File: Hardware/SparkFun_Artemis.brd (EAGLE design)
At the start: 15 x 10 mm, 75 parts, among them J1 PAD.4X.6, J10 PAD.4X.6, J11 PAD.4X.6, J12 PAD.4X.6, J13 PAD.4X.6, J14 PAD.4X.6, J15 PAD.4X.6, J16 PAD.4X.6, J17 PAD.4X.6, J18 PAD.4X.6, J19 PAD.4X.6, J2 PAD.4X.6, J20 PAD.4X.6, J21 PAD.4X.6, J22 PAD.4X.6, J23 PAD.4X.6, J24 PAD.4X.6, J25 PAD.4X.6, J26 PAD.4X.6, J27 PAD.4X.6, J28 PAD.4X.6, J29 PAD.4X.6, J3 PAD.4X.6, J30 PAD.4X.6, J31 PAD.4X.6, J32 PAD.4X.6, J34 PAD.4X.6, J35 PAD.4X.6, J36 PAD.4X.6, J37 PAD.4X.6, J38 PAD.4X.6, J39 PAD.4X.6, J4 PAD.4X.6, J40 PAD.4X.6, J41 PAD.4X.6, J42 PAD.4X.6, J43 PAD.4X.6, J44 PAD.4X.6, J45 PAD.4X.6, J46 PAD.35X.35, J47 PAD.4X.6, J48 PAD.4X.6, J49 PAD.4X.6, J5 PAD.4X.6, J6 PAD.4X.6, J7 PAD.4X.6, J8 PAD.4X.6, J9 PAD.4X.6, U1 AMBIQ-APOLLO3KBR, Y1 32MHz

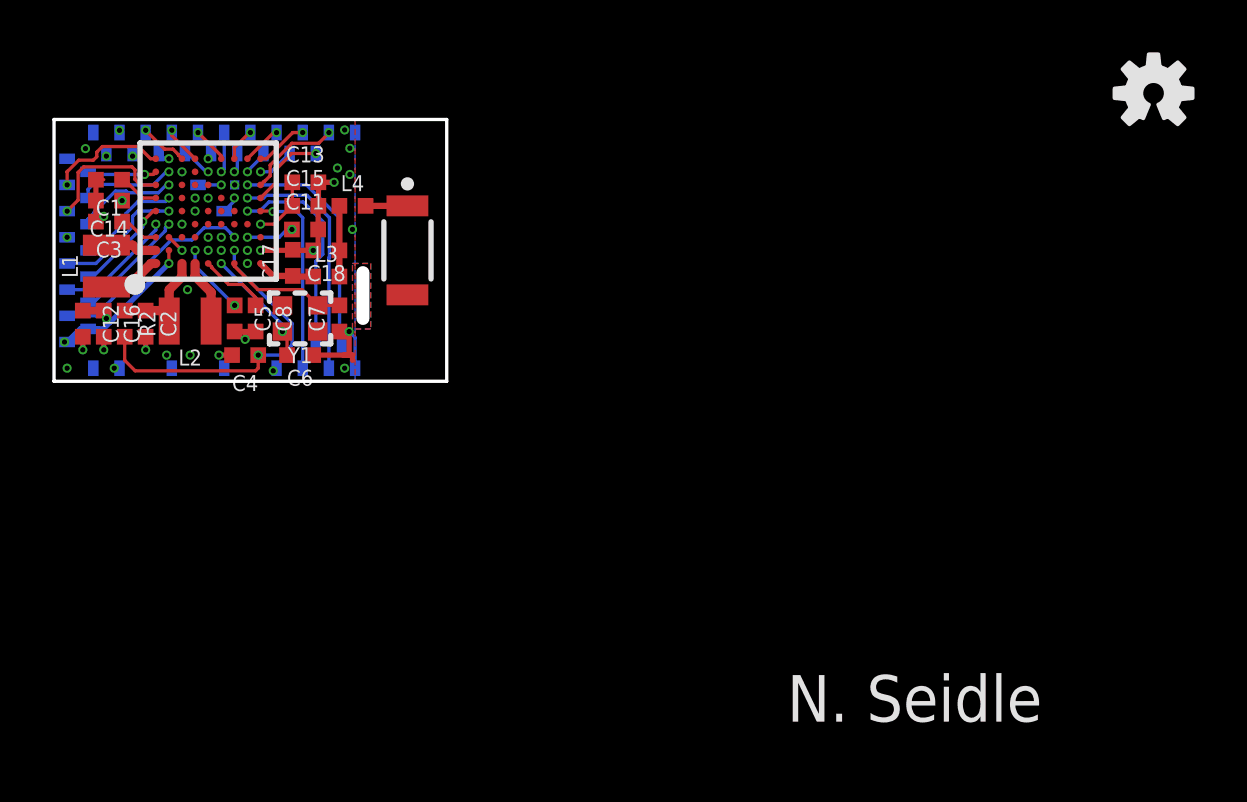
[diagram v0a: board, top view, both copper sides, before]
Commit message: Changing RF trace width to 11.55mil
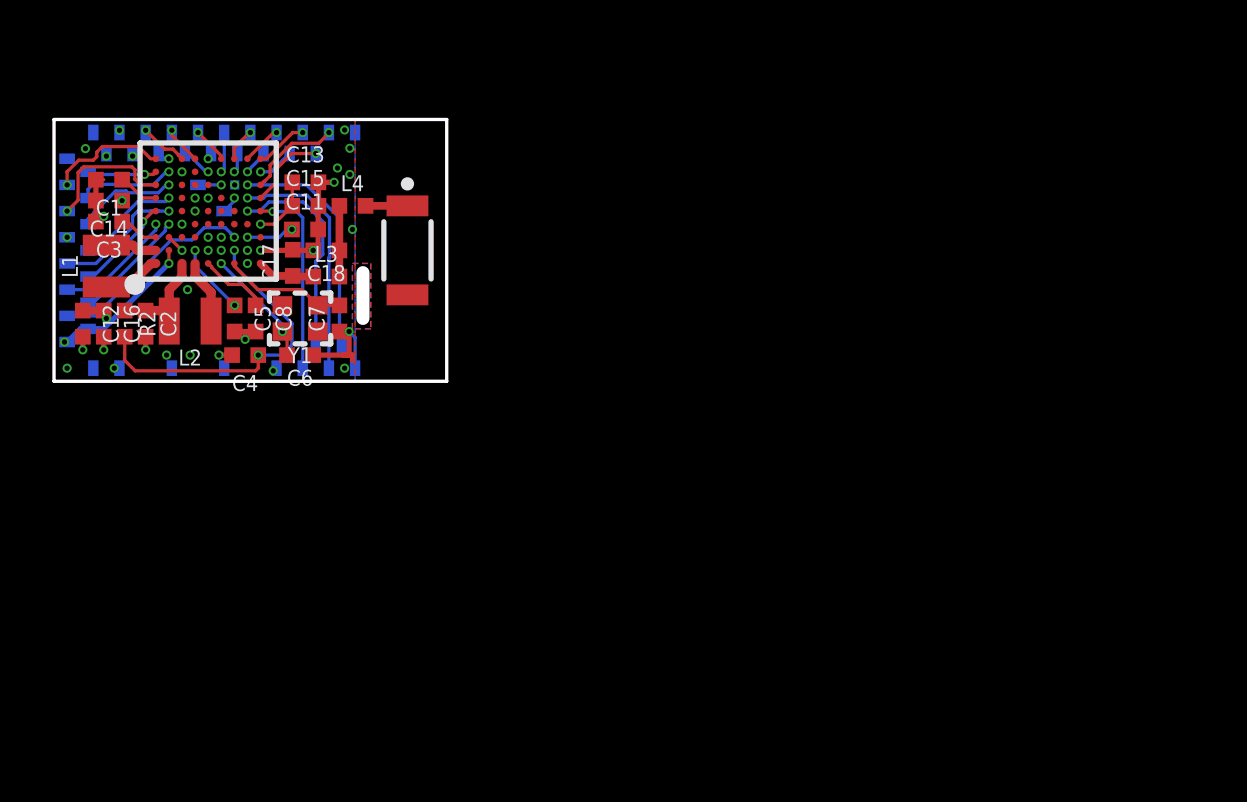
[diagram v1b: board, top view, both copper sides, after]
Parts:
- removed LOGO2: OSHW-LOGOS, SparkFun-Aesthetics:OSHW-LOGO-S
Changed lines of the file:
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@@
 <layer number="47" name="Measures" color="7" fill="1" visible="no" active="yes"/>
 <layer number="48" name="RF_Shield2" color="63" fill="1" visible="yes" active="yes"/>
-<layer number="49" name="Reference" color="7" fill="1" visible="yes" active="yes"/>
+<layer number="49" name="Reference" color="7" fill="1" visible="no" active="yes"/>
 <layer number="50" name="RF_Shield_Dimensions2" color="47" fill="1" visible="yes" active="yes"/>
 <layer number="51" name="tDocu" color="6" fill="1" visible="yes" active="yes"/>
@@
 <wire x1="11.8" y1="2.4" x2="11.8" y2="4.15" width="0.5" layer="46"/>
 <text x="40" y="5" size="1.778" layer="51" font="vector" ratio="15">0.8mm Thick FR4</text>
-<text x="28" y="-13" size="1.778" layer="21" font="vector" ratio="15">N. Seidle</text>
 <wire x1="0.4" y1="1" x2="0.4" y2="0.4" width="0.5" layer="48"/>
 <wire x1="0.4" y1="9.6" x2="0.4" y2="8.6" width="0.5" layer="48"/>
@@
 <wire x1="0.4" y1="0.4" x2="0.4" y2="9.6" width="0.05" layer="50"/>
 <text x="20.2" y="1.4" size="0.9" layer="50" font="vector" ratio="15">Alignment Leg Height: 1.8-1.9mm </text>
+<text x="27.559" y="-13.208" size="1.778" layer="51" font="vector" ratio="15">N. Seidle</text>
+<dimension x1="0.4" y1="1" x2="0.4" y2="0.4" x3="-2.3" y3="0.7" textsize="0.5" textratio="15" layer="50" width="0.05" unit="inch"/>
 </plain>
 <attributes>
@@
 <element name="J44" library="Module-Pads" package="MODULE_PAD" value="PAD.4X.6" x="0.5" y="8.5" smashed="yes" rot="MR0"/>
 <element name="LOGO1" library="SparkFun-Aesthetics" package="SFE_LOGO_FLAME_INTERNAL_0.05" value="SFE_LOGO_FLAME.05_INCH_INTERNAL" x="9.1" y="8.4" smashed="yes"/>
-<element name="LOGO2" library="SparkFun-Aesthetics" package="OSHW-LOGO-S" value="OSHW-LOGOS" x="42" y="11" smashed="yes"/>
 <element name="J46" library="Module-Pads" package="MODULE_MINI_PAD" value="PAD.35X.35" x="6.9" y="7.5" smashed="yes" rot="MR0"/>
 <element name="J45" library="Module-Pads" package="MODULE_PAD" value="PAD.4X.6" x="2.5" y="0.5" smashed="yes" rot="MR90"/>
@@
 <contactref element="C17" pad="1"/>
 <contactref element="L3" pad="1"/>
-<wire x1="7.888" y1="4.501" x2="8.366" y2="4.023" width="0.24" layer="1"/>
-<wire x1="8.366" y1="4.023" x2="9.121" y2="4.023" width="0.24" layer="1"/>
+<wire x1="7.888" y1="4.501" x2="8.366" y2="4.023" width="0.29336875" layer="1"/>
+<wire x1="8.366" y1="4.023" x2="9.121" y2="4.023" width="0.29336875" layer="1"/>
 <wire x1="9.121" y1="4.023" x2="9.144" y2="4" width="0.3048" layer="1"/>
-<wire x1="9.144" y1="4" x2="9.9" y2="4" width="0.24" layer="1"/>
+<wire x1="9.144" y1="4" x2="9.9" y2="4" width="0.29336875" layer="1"/>
 </signal>
 <signal name="VDDC">
@@
 <contactref element="L4" pad="1"/>
 <contactref element="C18" pad="1"/>
-<wire x1="10.9" y1="4" x2="10.9" y2="5" width="0.24" layer="1"/>
-<wire x1="10.9" y1="5" x2="10.9" y2="6.7" width="0.24" layer="1"/>
+<wire x1="10.9" y1="4" x2="10.9" y2="5" width="0.29336875" layer="1"/>
+<wire x1="10.9" y1="5" x2="10.9" y2="6.7" width="0.29336875" layer="1"/>
 </signal>
 <signal name="RXI-0">
@@
 <contactref element="L4" pad="2"/>
 <contactref element="A1" pad="FEED"/>
-<wire x1="11.9" y1="6.7" x2="13.5" y2="6.7" width="0.24" layer="1"/>
+<wire x1="11.9" y1="6.7" x2="13.5" y2="6.7" width="0.29336875" layer="1"/>
 </signal>
 <signal name="VDCDCRF">

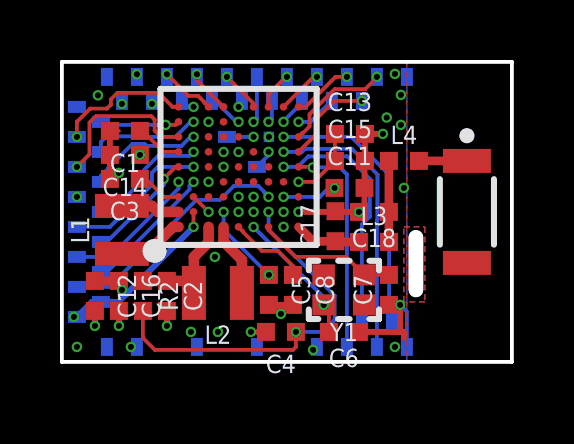
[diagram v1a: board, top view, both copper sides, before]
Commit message: Change chip antenna. Fixed shield running into trace. Post design review.
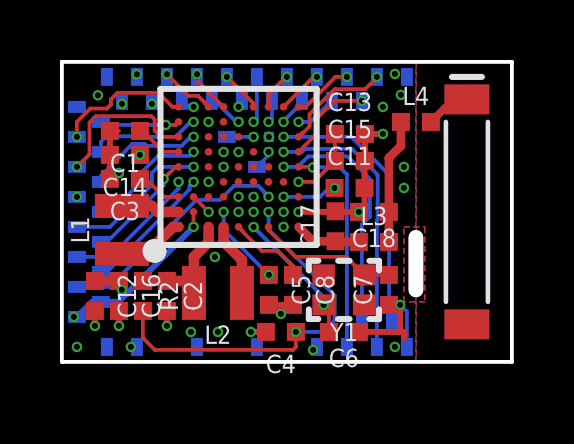
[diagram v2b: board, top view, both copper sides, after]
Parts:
- A1: device SparkFun-RF:ANT-2.4GHZ-3.2X1.6X1.2MM-REDUCED_KEEPOUT -> SparkFun-RF:ANT-2.4GHZ-8.0X1.0MM
- moved L4 1.36 mm to (11.8, 8.00)
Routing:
- net N$16: track 2.70 -> 4.17 mm
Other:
- board text added: "RF Shield: H:1.2mm Thickness: ~0.2mm"
- board text removed: "RF Shield: H:1.2mm"
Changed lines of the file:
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@@
 <layer number="47" name="Measures" color="7" fill="1" visible="no" active="yes"/>
 <layer number="48" name="RF_Shield2" color="63" fill="1" visible="yes" active="yes"/>
-<layer number="49" name="Reference" color="7" fill="1" visible="no" active="yes"/>
-<layer number="50" name="RF_Shield_Dimensions2" color="47" fill="1" visible="yes" active="yes"/>
+<layer number="49" name="Reference" color="7" fill="1" visible="yes" active="yes"/>
+<layer number="50" name="RF_Shield_Dimensions2" color="47" fill="1" visible="no" active="yes"/>
 <layer number="51" name="tDocu" color="6" fill="1" visible="yes" active="yes"/>
 <layer number="52" name="bDocu" color="29" fill="1" visible="no" active="yes"/>
@@
 <wire x1="11.8" y1="2.4" x2="11.8" y2="4.15" width="0.5" layer="46"/>
 <text x="40" y="5" size="1.778" layer="51" font="vector" ratio="15">0.8mm Thick FR4</text>
-<wire x1="0.4" y1="1" x2="0.4" y2="0.4" width="0.5" layer="48"/>
-<wire x1="0.4" y1="9.6" x2="0.4" y2="8.6" width="0.5" layer="48"/>
-<wire x1="0.4" y1="0.4" x2="3.1" y2="0.4" width="0.5" layer="48"/>
+<wire x1="0.4" y1="0.8" x2="0.4" y2="0.4" width="0.5" layer="48"/>
+<wire x1="0.4" y1="9.6" x2="0.4" y2="8.8" width="0.5" layer="48"/>
+<wire x1="0.4" y1="0.4" x2="1.2" y2="0.4" width="0.5" layer="48"/>
 <wire x1="0.4" y1="9.6" x2="1.4" y2="9.6" width="0.5" layer="48"/>
 <wire x1="11.8" y1="0.4" x2="10.8" y2="0.4" width="0.5" layer="48"/>
 <wire x1="11.1" y1="9.6" x2="11.8" y2="9.6" width="0.5" layer="48"/>
 <wire x1="11.8" y1="9.6" x2="11.8" y2="8.8" width="0.5" layer="48"/>
-<wire x1="0.4" y1="1" x2="0.4" y2="0.4" width="0.5" layer="29"/>
-<wire x1="0.4" y1="9.6" x2="0.4" y2="8.6" width="0.5" layer="29"/>
-<wire x1="0.4" y1="0.4" x2="3.1" y2="0.4" width="0.5" layer="29"/>
+<wire x1="0.4" y1="0.8" x2="0.4" y2="0.4" width="0.5" layer="29"/>
+<wire x1="0.4" y1="9.6" x2="0.4" y2="8.8" width="0.5" layer="29"/>
+<wire x1="0.4" y1="0.4" x2="1.195" y2="0.4" width="0.5" layer="29"/>
 <wire x1="0.4" y1="9.6" x2="1.4" y2="9.6" width="0.5" layer="29"/>
 <wire x1="11.8" y1="0.4" x2="10.8" y2="0.4" width="0.5" layer="29"/>
 <wire x1="11.1" y1="9.6" x2="11.8" y2="9.6" width="0.5" layer="29"/>
 <wire x1="11.8" y1="9.6" x2="11.8" y2="8.8" width="0.5" layer="29"/>
-<wire x1="0.4" y1="1" x2="0.4" y2="0.4" width="0.5" layer="31"/>
-<wire x1="0.4" y1="9.6" x2="0.4" y2="8.6" width="0.5" layer="31"/>
-<wire x1="0.4" y1="0.4" x2="3.1" y2="0.4" width="0.5" layer="31"/>
+<wire x1="0.4" y1="0.8" x2="0.4" y2="0.4" width="0.5" layer="31"/>
+<wire x1="0.4" y1="9.6" x2="0.4" y2="8.8" width="0.5" layer="31"/>
+<wire x1="0.4" y1="0.4" x2="1.2" y2="0.4" width="0.5" layer="31"/>
 <wire x1="0.4" y1="9.6" x2="1.4" y2="9.6" width="0.5" layer="31"/>
 <wire x1="11.8" y1="0.4" x2="10.8" y2="0.4" width="0.5" layer="31"/>
@@
 <dimension x1="0.4" y1="9.6" x2="1.4" y2="9.6" x3="0.9" y3="11.2" textsize="0.5" textratio="15" layer="50" dtype="vertical" width="0.05"/>
 <dimension x1="11.1" y1="9.6" x2="11.8" y2="9.6" x3="11.45" y3="10.6" textsize="0.5" textratio="15" layer="50" dtype="horizontal" width="0.05"/>
-<dimension x1="0.4" y1="0.4" x2="3.1" y2="0.4" x3="1.75" y3="-3.2" textsize="0.5" textratio="15" layer="50" dtype="horizontal" width="0.05"/>
+<dimension x1="0.4" y1="0.4" x2="1.2" y2="0.4" x3="0.8" y3="-3.2" textsize="0.5" textratio="15" layer="50" dtype="horizontal" width="0.05"/>
 <dimension x1="10.8" y1="0.4" x2="11.8" y2="0.4" x3="11.3" y3="-1.5" textsize="0.5" textratio="15" layer="50" dtype="horizontal" width="0.05"/>
 <dimension x1="11.8" y1="8.8" x2="11.8" y2="9.6" x3="16.2" y3="9.2" textsize="0.5" textratio="15" layer="50" dtype="horizontal" width="0.05"/>
@@
 <text x="-2" y="19" size="0.9" layer="50" font="vector" ratio="15">RF Shield:
   H:1.2mm
+  Thickness: ~0.2mm
 </text>
 <dimension x1="11.8" y1="2.4" x2="11.8" y2="4.15" x3="16.2" y3="3.275" textsize="0.5" textratio="15" layer="50" dtype="horizontal" width="0.05"/>
@@
 <wire x1="11.8" y1="0" x2="0" y2="0" width="0.127" layer="51"/>
 <rectangle x1="6.725" y1="7.325" x2="7.075" y2="7.675" layer="52" rot="R90"/>
-<wire x1="12.6" y1="6.7" x2="14.4" y2="6.7" width="0.127" layer="51"/>
-<wire x1="14.4" y1="6.7" x2="14.4" y2="3.3" width="0.127" layer="51"/>
-<wire x1="14.4" y1="3.3" x2="12.6" y2="3.3" width="0.127" layer="51"/>
-<wire x1="12.6" y1="3.3" x2="12.6" y2="6.7" width="0.127" layer="51"/>
+<wire x1="13" y1="9" x2="14" y2="9" width="0.127" layer="52"/>
+<wire x1="14" y1="9" x2="14" y2="1" width="0.127" layer="52"/>
+<wire x1="14" y1="1" x2="13" y2="1" width="0.127" layer="52"/>
+<wire x1="13" y1="1" x2="13" y2="9" width="0.127" layer="52"/>
 <wire x1="11.8" y1="0" x2="11.8" y2="10" width="0.127" layer="51"/>
 <text x="11.5" y="9.5" size="0.2" layer="49" font="vector" ratio="15" align="center">1</text>
@@
 <text x="20.2" y="1.4" size="0.9" layer="50" font="vector" ratio="15">Alignment Leg Height: 1.8-1.9mm </text>
 <text x="27.559" y="-13.208" size="1.778" layer="51" font="vector" ratio="15">N. Seidle</text>
-<dimension x1="0.4" y1="1" x2="0.4" y2="0.4" x3="-2.3" y3="0.7" textsize="0.5" textratio="15" layer="50" width="0.05" unit="inch"/>
+<dimension x1="0.4" y1="0.8" x2="0.4" y2="0.4" x3="-2.3" y3="0.6" textsize="0.5" textratio="15" layer="50" width="0.05"/>
+<dimension x1="0.4" y1="9.6" x2="0.4" y2="8.8" x3="-2.6" y3="9.2" textsize="0.5" textratio="15" layer="50" width="0.05"/>
+<dimension x1="12.1" y1="2.2" x2="12.1" y2="4.4" x3="18" y3="3.3" textsize="0.5" textratio="15" layer="50" width="0.05"/>
+<dimension x1="0.4" y1="9.8" x2="0.4" y2="8.6" x3="-5.6" y3="9.2" textsize="0.5" textratio="15" layer="50" width="0.05"/>
+<wire x1="0" y1="0" x2="0" y2="1.05" width="0.05" layer="50"/>
 </plain>
 <attributes>
@@
 <attribute name="VALUE" x="9.5008" y="4.9918" size="0.6096" layer="27" font="vector" ratio="20" rot="R270" align="top-center"/>
 </element>
-<element name="L4" library="SparkFun-Coils" package="0402-TIGHT" value="2nH/?%/200mA/300mOhm" x="11.4" y="6.7" smashed="yes">
-<attribute name="NAME" x="11.4" y="7.262" size="0.6096" layer="25" font="vector" ratio="20" align="bottom-center"/>
-<attribute name="PROD_ID" value="NDUC-14238" x="11.4" y="6.7" size="1.778" layer="27" display="off"/>
-<attribute name="VALUE" value="2nH/?%/200mA/300mOhm" x="11.8724" y="7.1014" size="0.6096" layer="27" font="vector" ratio="20" rot="R180" align="top-center"/>
-</element>
-<element name="A1" library="SparkFun-RF" package="ANT-2.4GHZ-3.2X1.6X1.2MM-REDUCED_KEEPOUT" value="2.4GHZ-3.2X1.6MM" x="13.5" y="5" smashed="yes" rot="R270">
-<attribute name="PROD_ID" value="ANT-14235" x="13.5" y="5" size="1.778" layer="27" rot="R270" display="off"/>
+<element name="L4" library="SparkFun-Coils" package="0402-TIGHT" value="2nH/?%/200mA/300mOhm" x="11.8" y="8" smashed="yes">
+<attribute name="NAME" x="11.8" y="8.562" size="0.6096" layer="25" font="vector" ratio="20" align="bottom-center"/>
+<attribute name="PROD_ID" value="NDUC-14238" x="11.8" y="8" size="1.778" layer="27" display="off"/>
+<attribute name="VALUE" value="2nH/?%/200mA/300mOhm" x="12.2724" y="8.4014" size="0.6096" layer="27" font="vector" ratio="20" rot="R180" align="top-center"/>
+</element>
+<element name="A1" library="SparkFun-RF" package="ANT-2.4GHZ-8.0X1.0MM" value="2.4GHZ-3.2X1.6MM" x="13.5" y="5" smashed="yes" rot="R270">
+<attribute name="PROD_ID" value="ANT-11807" x="13.5" y="5" size="1.778" layer="27" rot="R270" display="off"/>
 </element>
 <element name="R2" library="SparkFun-Resistors" package="0402-TIGHT" value="0" x="2.7" y="2.2" smashed="yes" rot="R270">
@@
 <vertex x="0" y="10"/>
 <vertex x="0" y="0"/>
-<vertex x="11.5" y="0"/>
-<vertex x="11.5" y="10"/>
+<vertex x="11.8" y="0"/>
+<vertex x="11.8" y="10"/>
 </polygon>
 <contactref element="J24" pad="1"/>
@@
 <wire x1="11.049" y1="1" x2="11.273" y2="1" width="0.2" layer="1"/>
 <polygon width="0.127" layer="1" isolate="0.127">
-<vertex x="11.5" y="10"/>
-<vertex x="11.5" y="0"/>
+<vertex x="11.808" y="10"/>
+<vertex x="11.808" y="0"/>
 <vertex x="0" y="0"/>
 <vertex x="0" y="10"/>
@@
 <via x="5.2" y="1" extent="1-16" drill="0.2"/>
 <via x="5.1" y="3.5" extent="1-16" drill="0.2"/>
-<via x="10.827" y="8.146" extent="1-16" drill="0.2"/>
-<via x="11.3" y="7.9" extent="1-16" drill="0.2"/>
+<via x="10.7" y="8.5" extent="1-16" drill="0.2"/>
+<via x="11.4" y="6.5" extent="1-16" drill="0.2"/>
 <via x="11.4" y="5.8" extent="1-16" drill="0.2"/>
 <via x="11.1" y="0.5" extent="1-16" drill="0.2"/>
@@
 <contactref element="C18" pad="1"/>
 <wire x1="10.9" y1="4" x2="10.9" y2="5" width="0.29336875" layer="1"/>
-<wire x1="10.9" y1="5" x2="10.9" y2="6.7" width="0.29336875" layer="1"/>
+<wire x1="11.3" y1="8" x2="11.3" y2="7.2" width="0.29336875" layer="1"/>
+<wire x1="11.3" y1="7.2" x2="10.9" y2="6.8" width="0.29336875" layer="1"/>
+<wire x1="10.9" y1="5" x2="10.9" y2="6.8" width="0.29336875" layer="1"/>
 </signal>
 <signal name="RXI-0">
@@
 <contactref element="L4" pad="2"/>
 <contactref element="A1" pad="FEED"/>
-<wire x1="11.9" y1="6.7" x2="13.5" y2="6.7" width="0.29336875" layer="1"/>
+<wire x1="13.5" y1="8.75" x2="13.05" y2="8.75" width="0.254" layer="1"/>
+<wire x1="13.05" y1="8.75" x2="12.3" y2="8" width="0.254" layer="1"/>
 </signal>
 <signal name="VDCDCRF">
@@
 <contactref element="J14" pad="1"/>
 <via x="0.5" y="7.5" extent="1-16" drill="0.2"/>
-<wire x1="0.5" y1="8.0186" x2="0.5" y2="8" width="0.127" layer="1"/>
 <wire x1="0.5" y1="8" x2="0.5" y2="7.5" width="0.127" layer="1"/>
 <wire x1="3.888" y1="8.501" x2="3.688" y2="8.501" width="0.127" layer="1"/>
